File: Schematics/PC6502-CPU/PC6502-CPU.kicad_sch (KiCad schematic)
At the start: 62 parts, among them J1 BUS, J4 TEST, J5 Conn_02x05_Odd_Even, J6 Conn_02x02_Odd_Even, U2 AS6C4008-55PCN, U3 SST39SF010, U4 ATF1502AS, U5 W65C02, U6 74AHC244, U8 MCP130-450DI/TO, X1 CXO_DIP8

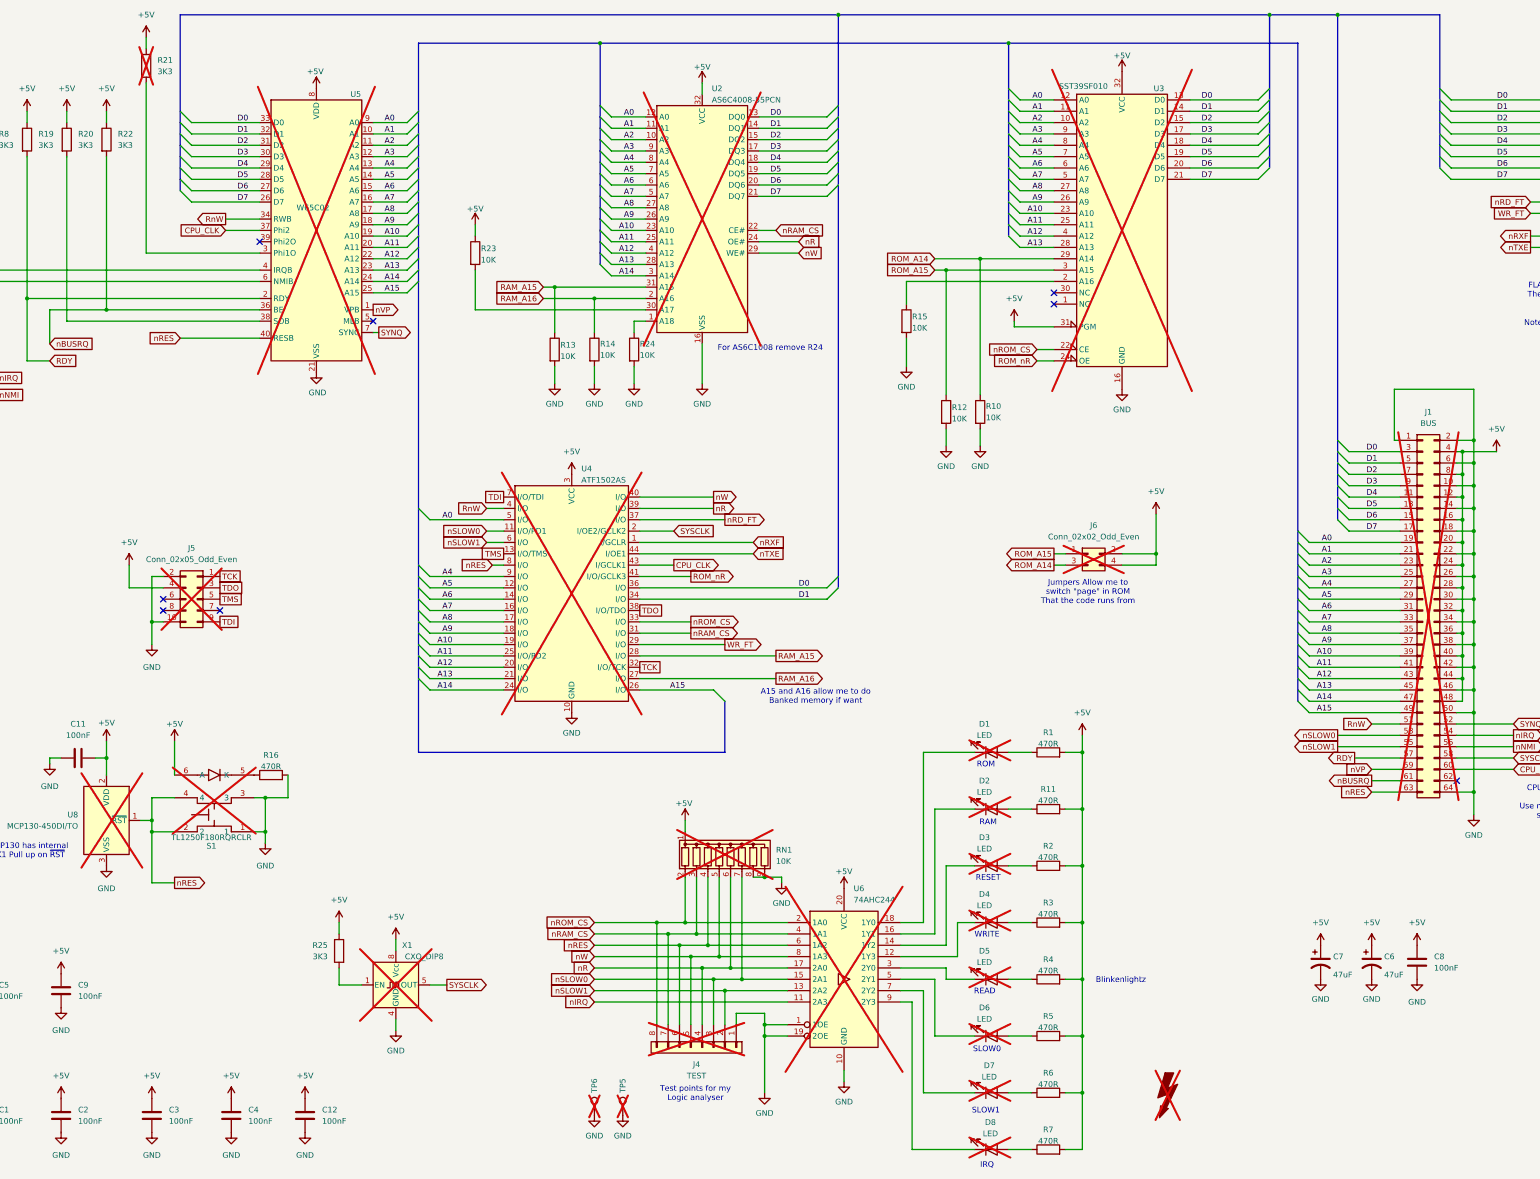
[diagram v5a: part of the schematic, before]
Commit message: Tidy up and simplify
Created schematic for FM & Speech sound board
Made Storage board just for Compact Flash (CF) storage
Routed Storage PCB
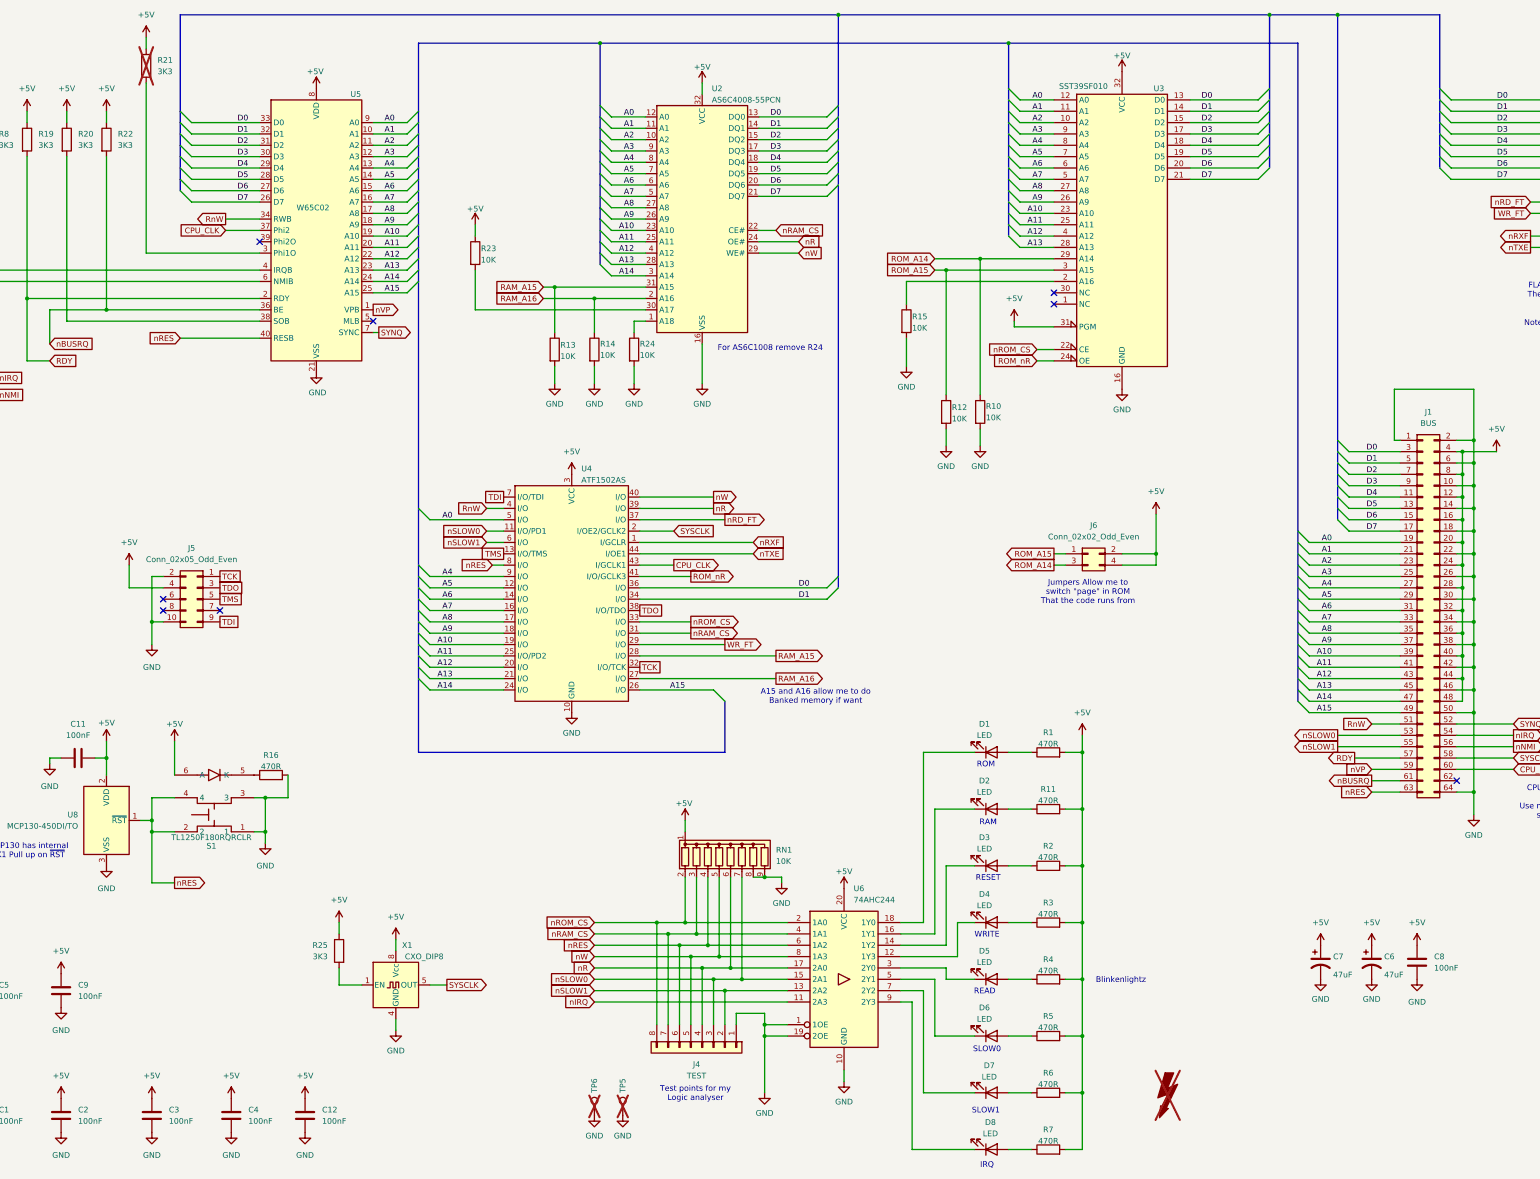
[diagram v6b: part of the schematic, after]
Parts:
- D1, D2, D3, D4, D5, D6, D7, D8, J1, J4, J5, J6, RN1, S1, U2, U3, U4, U5, U6, U8, X1: now fitted
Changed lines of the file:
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@@
 		(in_bom yes)
 		(on_board yes)
-		(dnp yes)
+		(dnp no)
 		(fields_autoplaced yes)
 		(property "Reference" "D2"
@@
 		(in_bom yes)
 		(on_board yes)
-		(dnp yes)
+		(dnp no)
 		(property "Reference" "U5"
 			(at 106.68 36.83 0)
@@
 		(in_bom yes)
 		(on_board yes)
-		(dnp yes)
+		(dnp no)
 		(fields_autoplaced yes)
 		(property "Reference" "U8"
@@
 		(in_bom yes)
 		(on_board yes)
-		(dnp yes)
+		(dnp no)
 		(property "Reference" "D8"
 			(at 249.936 266.954 0)
@@
 		(in_bom yes)
 		(on_board yes)
-		(dnp yes)
+		(dnp no)
 		(fields_autoplaced yes)
 		(property "Reference" "U4"
@@
 		(in_bom yes)
 		(on_board yes)
-		(dnp yes)
+		(dnp no)
 		(fields_autoplaced yes)
 		(property "Reference" "J5"
@@
 		(in_bom yes)
 		(on_board yes)
-		(dnp yes)
+		(dnp no)
 		(fields_autoplaced yes)
 		(property "Reference" "U2"
@@
 		(in_bom yes)
 		(on_board yes)
-		(dnp yes)
+		(dnp no)
 		(fields_autoplaced yes)
 		(property "Reference" "U6"
@@
 		(in_bom yes)
 		(on_board yes)
-		(dnp yes)
+		(dnp no)
 		(property "Reference" "D7"
 			(at 249.682 254.254 0)
@@
 		(in_bom yes)
 		(on_board yes)
-		(dnp yes)
+		(dnp no)
 		(fields_autoplaced yes)
 		(property "Reference" "D3"
@@
 		(in_bom yes)
 		(on_board yes)
-		(dnp yes)
+		(dnp no)
 		(fields_autoplaced yes)
 		(property "Reference" "J6"
@@
 		(in_bom yes)
 		(on_board yes)
-		(dnp yes)
+		(dnp no)
 		(property "Reference" "S1"
 			(at 75.565 205.105 0)
@@
 		(in_bom yes)
 		(on_board yes)
-		(dnp yes)
+		(dnp no)
 		(property "Reference" "J1"
 			(at 347.98 107.95 0)
@@
 		(in_bom yes)
 		(on_board yes)
-		(dnp yes)
+		(dnp no)
 		(property "Reference" "U3"
 			(at 287.655 35.56 0)
@@
 		(in_bom yes)
 		(on_board yes)
-		(dnp yes)
+		(dnp no)
 		(fields_autoplaced yes)
 		(property "Reference" "D6"
@@
 		(in_bom yes)
 		(on_board yes)
-		(dnp yes)
+		(dnp no)
 		(fields_autoplaced yes)
 		(property "Reference" "J4"
@@
 		(in_bom yes)
 		(on_board yes)
-		(dnp yes)
+		(dnp no)
 		(fields_autoplaced yes)
 		(property "Reference" "D1"
@@
 		(in_bom yes)
 		(on_board yes)
-		(dnp yes)
+		(dnp no)
 		(fields_autoplaced yes)
 		(property "Reference" "RN1"
@@
 		(in_bom yes)
 		(on_board yes)
-		(dnp yes)
+		(dnp no)
 		(fields_autoplaced yes)
 		(property "Reference" "D4"
@@
 		(in_bom yes)
 		(on_board yes)
-		(dnp yes)
+		(dnp no)
 		(fields_autoplaced yes)
 		(property "Reference" "D5"
@@
 		(in_bom yes)
 		(on_board yes)
-		(dnp yes)
+		(dnp no)
 		(property "Reference" "X1"
 			(at 119.38 227.33 0)

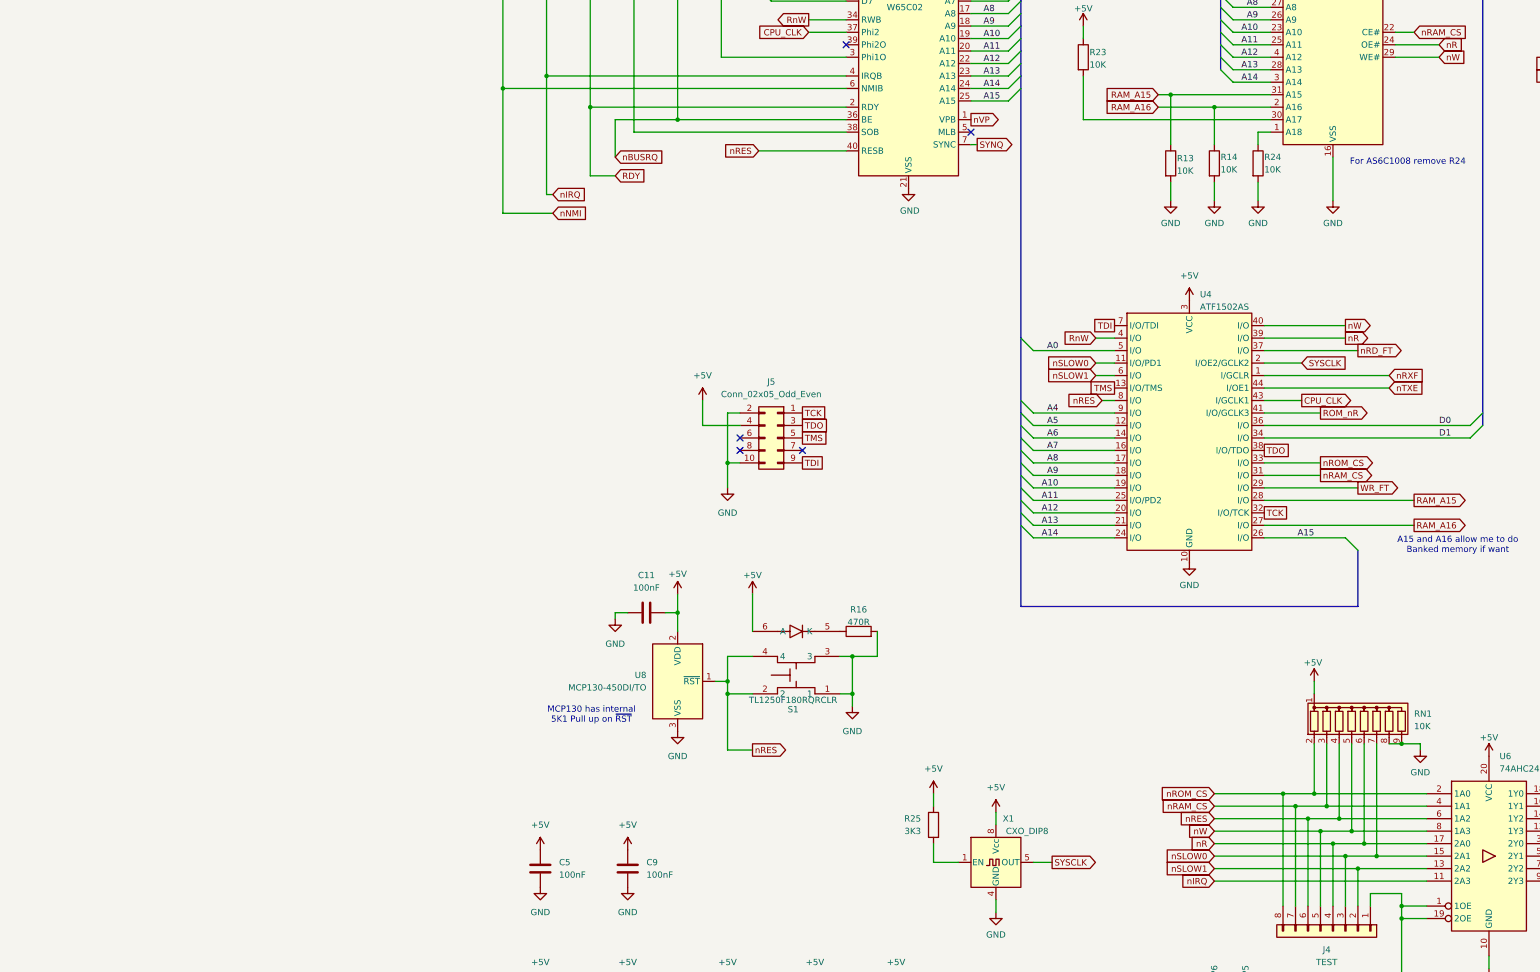
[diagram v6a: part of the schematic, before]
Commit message: Updated following testing
New CPLD code for CPU and VIA
Fixed mistakes with CPU Board and upped to Rev 1.2 (My Rev 1.1 has mods on)
Updated README
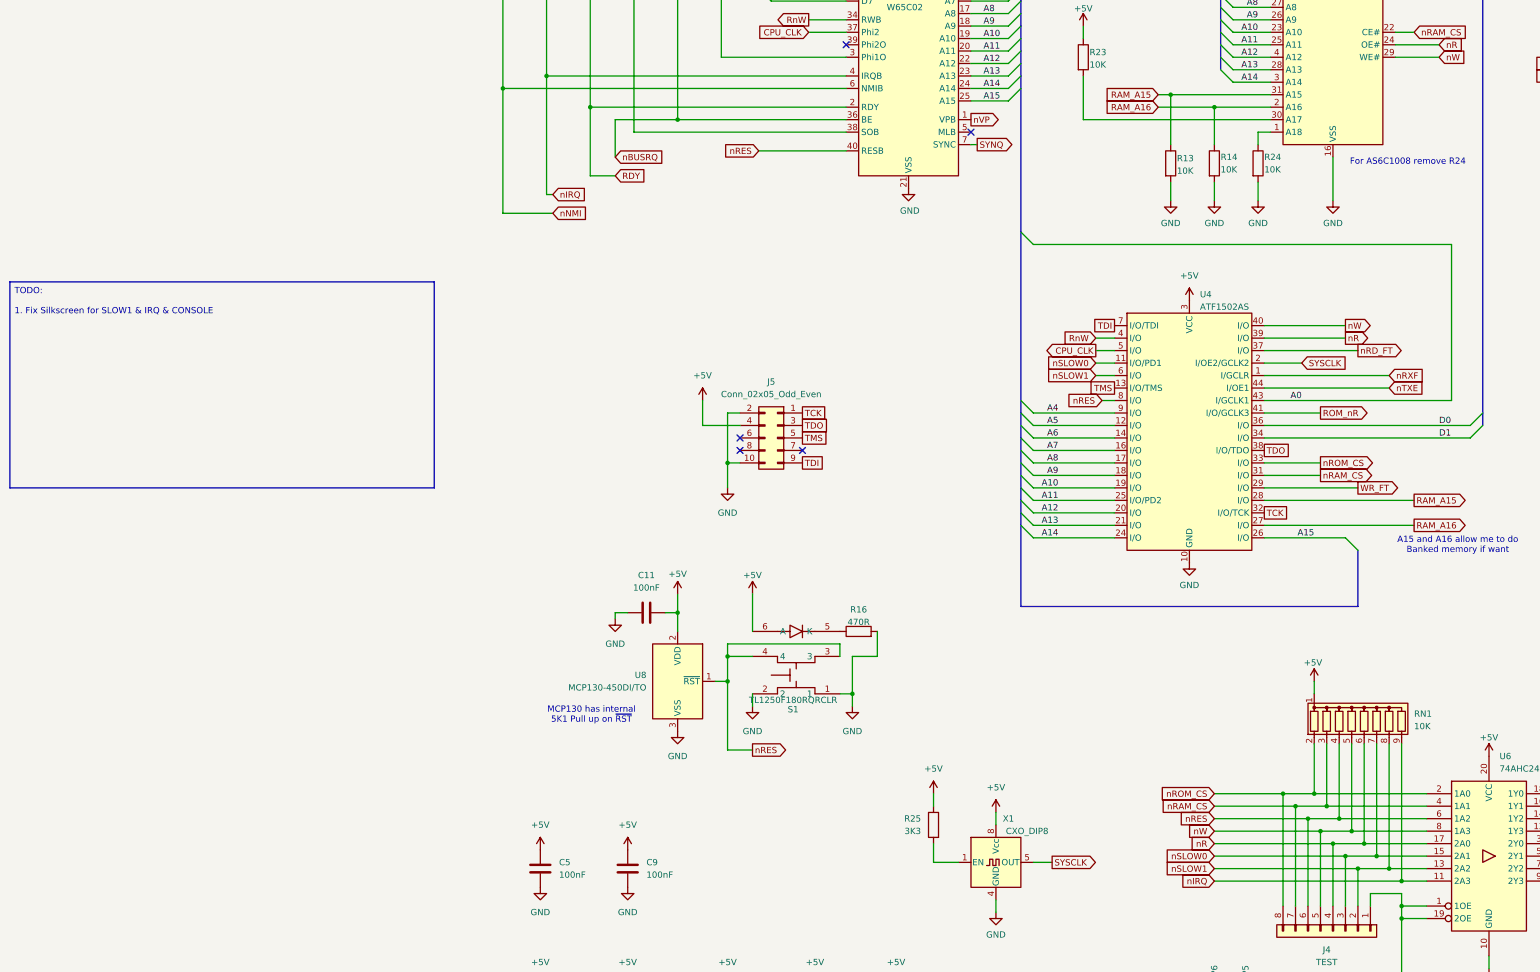
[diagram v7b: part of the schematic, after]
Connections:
- net A0: now also U4.43 (I/GCLK1); no longer U4.5 (I/O)
- net CPU_CLK: now also U4.5 (I/O); no longer U4.43 (I/GCLK1)
- net GND: now also S1.2; no longer RN1.8 (R7), RN1.9 (R8), S1.3
- net nIRQ: now also RN1.9 (R8)
- net nRES: now also S1.3; no longer S1.2
- net nSLOW1: now also RN1.8 (R7)
